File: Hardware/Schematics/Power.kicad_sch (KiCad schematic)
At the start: 26 parts, among them J7 USB_B_Micro, J8 Conn_01x02, U5 MT3608, U6 BQ25071, U7 TPS63900, U9 WE-TVS-82400102

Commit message: title block update
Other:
- title: Water Analyser Power -> LoRa Node Power
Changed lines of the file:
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@@
 	(paper "A4")
 	(title_block
-		(title "Water Analyser Power")
+		(title "LoRa Node Power")
 		(date "2025-11-28")
 		(rev "A")
@@
 		)
 		(instances
-			(project "demo wateranalyser"
+			(project "demo LoRa_Node"
 				(path "/3e989608-eeda-4a48-bc6c-c5e1d1678702/98bcb7c1-a14b-48e1-9268-def1b948ddb6"
 					(reference "#PWR061")
@@
 		)
 		(instances
-			(project "demo wateranalyser"
+			(project "demo LoRa_Node"
 				(path "/3e989608-eeda-4a48-bc6c-c5e1d1678702/98bcb7c1-a14b-48e1-9268-def1b948ddb6"
 					(reference "U6")
@@
 		)
 		(instances
-			(project "demo wateranalyser"
+			(project "demo LoRa_Node"
 				(path "/3e989608-eeda-4a48-bc6c-c5e1d1678702/98bcb7c1-a14b-48e1-9268-def1b948ddb6"
 					(reference "U9")
@@
 		)
 		(instances
-			(project "demo wateranalyser"
+			(project "demo LoRa_Node"
 				(path "/3e989608-eeda-4a48-bc6c-c5e1d1678702/98bcb7c1-a14b-48e1-9268-def1b948ddb6"
 					(reference "#PWR058")
@@
 		)
 		(instances
-			(project "demo wateranalyser"
+			(project "demo LoRa_Node"
 				(path "/3e989608-eeda-4a48-bc6c-c5e1d1678702/98bcb7c1-a14b-48e1-9268-def1b948ddb6"
 					(reference "#FLG01")
@@
 		)
 		(instances
-			(project "demo wateranalyser"
+			(project "demo LoRa_Node"
 				(path "/3e989608-eeda-4a48-bc6c-c5e1d1678702/98bcb7c1-a14b-48e1-9268-def1b948ddb6"
 					(reference "BT1")
@@
 		)
 		(instances
-			(project "demo wateranalyser"
+			(project "demo LoRa_Node"
 				(path "/3e989608-eeda-4a48-bc6c-c5e1d1678702/98bcb7c1-a14b-48e1-9268-def1b948ddb6"
 					(reference "R22")
@@
 		)
 		(instances
-			(project "demo wateranalyser"
+			(project "demo LoRa_Node"
 				(path "/3e989608-eeda-4a48-bc6c-c5e1d1678702/98bcb7c1-a14b-48e1-9268-def1b948ddb6"
 					(reference "C35")
@@
 		)
 		(instances
-			(project "demo wateranalyser"
+			(project "demo LoRa_Node"
 				(path "/3e989608-eeda-4a48-bc6c-c5e1d1678702/98bcb7c1-a14b-48e1-9268-def1b948ddb6"
 					(reference "#PWR064")
@@
 		)
 		(instances
-			(project "demo wateranalyser"
+			(project "demo LoRa_Node"
 				(path "/3e989608-eeda-4a48-bc6c-c5e1d1678702/98bcb7c1-a14b-48e1-9268-def1b948ddb6"
 					(reference "#PWR056")
@@
 		)
 		(instances
-			(project "demo wateranalyser"
+			(project "demo LoRa_Node"
 				(path "/3e989608-eeda-4a48-bc6c-c5e1d1678702/98bcb7c1-a14b-48e1-9268-def1b948ddb6"
 					(reference "#PWR055")
@@
 		)
 		(instances
-			(project "demo wateranalyser"
+			(project "demo LoRa_Node"
 				(path "/3e989608-eeda-4a48-bc6c-c5e1d1678702/98bcb7c1-a14b-48e1-9268-def1b948ddb6"
 					(reference "L7")
@@
 		)
 		(instances
-			(project "demo wateranalyser"
+			(project "demo LoRa_Node"
 				(path "/3e989608-eeda-4a48-bc6c-c5e1d1678702/98bcb7c1-a14b-48e1-9268-def1b948ddb6"
 					(reference "D9")
@@
 		)
 		(instances
-			(project "demo wateranalyser"
+			(project "demo LoRa_Node"
 				(path "/3e989608-eeda-4a48-bc6c-c5e1d1678702/98bcb7c1-a14b-48e1-9268-def1b948ddb6"
 					(reference "#PWR050")
@@
 		)
 		(instances
-			(project "demo wateranalyser"
+			(project "demo LoRa_Node"
 				(path "/3e989608-eeda-4a48-bc6c-c5e1d1678702/98bcb7c1-a14b-48e1-9268-def1b948ddb6"
 					(reference "#PWR057")
@@
 		)
 		(instances
-			(project "demo wateranalyser"
+			(project "demo LoRa_Node"
 				(path "/3e989608-eeda-4a48-bc6c-c5e1d1678702/98bcb7c1-a14b-48e1-9268-def1b948ddb6"
 					(reference "#FLG04")
@@
 		)
 		(instances
-			(project "demo wateranalyser"
+			(project "demo LoRa_Node"
 				(path "/3e989608-eeda-4a48-bc6c-c5e1d1678702/98bcb7c1-a14b-48e1-9268-def1b948ddb6"
 					(reference "R24")
@@
 		)
 		(instances
-			(project "demo wateranalyser"
+			(project "demo LoRa_Node"
 				(path "/3e989608-eeda-4a48-bc6c-c5e1d1678702/98bcb7c1-a14b-48e1-9268-def1b948ddb6"
 					(reference "R21")
@@
 		)
 		(instances
-			(project "demo wateranalyser"
+			(project "demo LoRa_Node"
 				(path "/3e989608-eeda-4a48-bc6c-c5e1d1678702/98bcb7c1-a14b-48e1-9268-def1b948ddb6"
 					(reference "#PWR048")
@@
 		)
 		(instances
-			(project "demo wateranalyser"
+			(project "demo LoRa_Node"
 				(path "/3e989608-eeda-4a48-bc6c-c5e1d1678702/98bcb7c1-a14b-48e1-9268-def1b948ddb6"
 					(reference "U7")
@@
 		)
 		(instances
-			(project "demo wateranalyser"
+			(project "demo LoRa_Node"
 				(path "/3e989608-eeda-4a48-bc6c-c5e1d1678702/98bcb7c1-a14b-48e1-9268-def1b948ddb6"
 					(reference "J7")
@@
 		)
 		(instances
-			(project "demo wateranalyser"
+			(project "demo LoRa_Node"
 				(path "/3e989608-eeda-4a48-bc6c-c5e1d1678702/98bcb7c1-a14b-48e1-9268-def1b948ddb6"
 					(reference "#PWR053")
@@
 		)
 		(instances
-			(project "demo wateranalyser"
+			(project "demo LoRa_Node"
 				(path "/3e989608-eeda-4a48-bc6c-c5e1d1678702/98bcb7c1-a14b-48e1-9268-def1b948ddb6"
 					(reference "#PWR047")
@@
 		)
 		(instances
-			(project "demo wateranalyser"
+			(project "demo LoRa_Node"
 				(path "/3e989608-eeda-4a48-bc6c-c5e1d1678702/98bcb7c1-a14b-48e1-9268-def1b948ddb6"
 					(reference "R19")
@@
 		)
 		(instances
-			(project "demo wateranalyser"
+			(project "demo LoRa_Node"
 				(path "/3e989608-eeda-4a48-bc6c-c5e1d1678702/98bcb7c1-a14b-48e1-9268-def1b948ddb6"
 					(reference "D8")
@@
 		)
 		(instances
-			(project "demo wateranalyser"
+			(project "demo LoRa_Node"
 				(path "/3e989608-eeda-4a48-bc6c-c5e1d1678702/98bcb7c1-a14b-48e1-9268-def1b948ddb6"
 					(reference "#PWR051")
@@
 		)
 		(instances
-			(project "demo wateranalyser"
+			(project "demo LoRa_Node"
 				(path "/3e989608-eeda-4a48-bc6c-c5e1d1678702/98bcb7c1-a14b-48e1-9268-def1b948ddb6"
 					(reference "#PWR060")
@@
 		)
 		(instances
-			(project "demo wateranalyser"
+			(project "demo LoRa_Node"
 				(path "/3e989608-eeda-4a48-bc6c-c5e1d1678702/98bcb7c1-a14b-48e1-9268-def1b948ddb6"
 					(reference "C34")
@@
 		)
 		(instances
-			(project "demo wateranalyser"
+			(project "demo LoRa_Node"
 				(path "/3e989608-eeda-4a48-bc6c-c5e1d1678702/98bcb7c1-a14b-48e1-9268-def1b948ddb6"
 					(reference "C37")
@@
 		)
 		(instances
-			(project "demo wateranalyser"
+			(project "demo LoRa_Node"
 				(path "/3e989608-eeda-4a48-bc6c-c5e1d1678702/98bcb7c1-a14b-48e1-9268-def1b948ddb6"
 					(reference "#PWR054")
@@
 		)
 		(instances
-			(project "demo wateranalyser"
+			(project "demo LoRa_Node"
 				(path "/3e989608-eeda-4a48-bc6c-c5e1d1678702/98bcb7c1-a14b-48e1-9268-def1b948ddb6"
 					(reference "#PWR049")
@@
 		)
 		(instances
-			(project "demo wateranalyser"
+			(project "demo LoRa_Node"
 				(path "/3e989608-eeda-4a48-bc6c-c5e1d1678702/98bcb7c1-a14b-48e1-9268-def1b948ddb6"
 					(reference "C32")
@@
 		)
 		(instances
-			(project "demo wateranalyser"
+			(project "demo LoRa_Node"
 				(path "/3e989608-eeda-4a48-bc6c-c5e1d1678702/98bcb7c1-a14b-48e1-9268-def1b948ddb6"
 					(reference "#PWR063")
@@
 		)
 		(instances
-			(project "demo wateranalyser"
+			(project "demo LoRa_Node"
 				(path "/3e989608-eeda-4a48-bc6c-c5e1d1678702/98bcb7c1-a14b-48e1-9268-def1b948ddb6"
 					(reference "R25")
@@
 		)
 		(instances
-			(project "demo wateranalyser"
+			(project "demo LoRa_Node"
 				(path "/3e989608-eeda-4a48-bc6c-c5e1d1678702/98bcb7c1-a14b-48e1-9268-def1b948ddb6"
 					(reference "#PWR052")
@@
 		)
 		(instances
-			(project "demo wateranalyser"
+			(project "demo LoRa_Node"
 				(path "/3e989608-eeda-4a48-bc6c-c5e1d1678702/98bcb7c1-a14b-48e1-9268-def1b948ddb6"
 					(reference "J8")
@@
 		)
 		(instances
-			(project "demo wateranalyser"
+			(project "demo LoRa_Node"
 				(path "/3e989608-eeda-4a48-bc6c-c5e1d1678702/98bcb7c1-a14b-48e1-9268-def1b948ddb6"
 					(reference "R20")
@@
 		)
 		(instances
-			(project "demo wateranalyser"
+			(project "demo LoRa_Node"
 				(path "/3e989608-eeda-4a48-bc6c-c5e1d1678702/98bcb7c1-a14b-48e1-9268-def1b948ddb6"
 					(reference "R27")
@@
 		)
 		(instances
-			(project "demo wateranalyser"
+			(project "demo LoRa_Node"
 				(path "/3e989608-eeda-4a48-bc6c-c5e1d1678702/98bcb7c1-a14b-48e1-9268-def1b948ddb6"
 					(reference "#PWR062")
@@
 		)
 		(instances
-			(project "demo wateranalyser"
+			(project "demo LoRa_Node"
 				(path "/3e989608-eeda-4a48-bc6c-c5e1d1678702/98bcb7c1-a14b-48e1-9268-def1b948ddb6"
 					(reference "#PWR059")
@@
 		)
 		(instances
-			(project "demo wateranalyser"
+			(project "demo LoRa_Node"
 				(path "/3e989608-eeda-4a48-bc6c-c5e1d1678702/98bcb7c1-a14b-48e1-9268-def1b948ddb6"
 					(reference "L8")
@@
 		)
 		(instances
-			(project "demo wateranalyser"
+			(project "demo LoRa_Node"
 				(path "/3e989608-eeda-4a48-bc6c-c5e1d1678702/98bcb7c1-a14b-48e1-9268-def1b948ddb6"
 					(reference "U5")
@@
 		)
 		(instances
-			(project "demo wateranalyser"
+			(project "demo LoRa_Node"
 				(path "/3e989608-eeda-4a48-bc6c-c5e1d1678702/98bcb7c1-a14b-48e1-9268-def1b948ddb6"
 					(reference "C38")
@@
 		)
 		(instances
-			(project "demo wateranalyser"
+			(project "demo LoRa_Node"
 				(path "/3e989608-eeda-4a48-bc6c-c5e1d1678702/98bcb7c1-a14b-48e1-9268-def1b948ddb6"
 					(reference "C36")
@@
 		)
 		(instances
-			(project "demo wateranalyser"
+			(project "demo LoRa_Node"
 				(path "/3e989608-eeda-4a48-bc6c-c5e1d1678702/98bcb7c1-a14b-48e1-9268-def1b948ddb6"
 					(reference "C33")
@@
 		)
 		(instances
-			(project "demo wateranalyser"
+			(project "demo LoRa_Node"
 				(path "/3e989608-eeda-4a48-bc6c-c5e1d1678702/98bcb7c1-a14b-48e1-9268-def1b948ddb6"
 					(reference "R23")

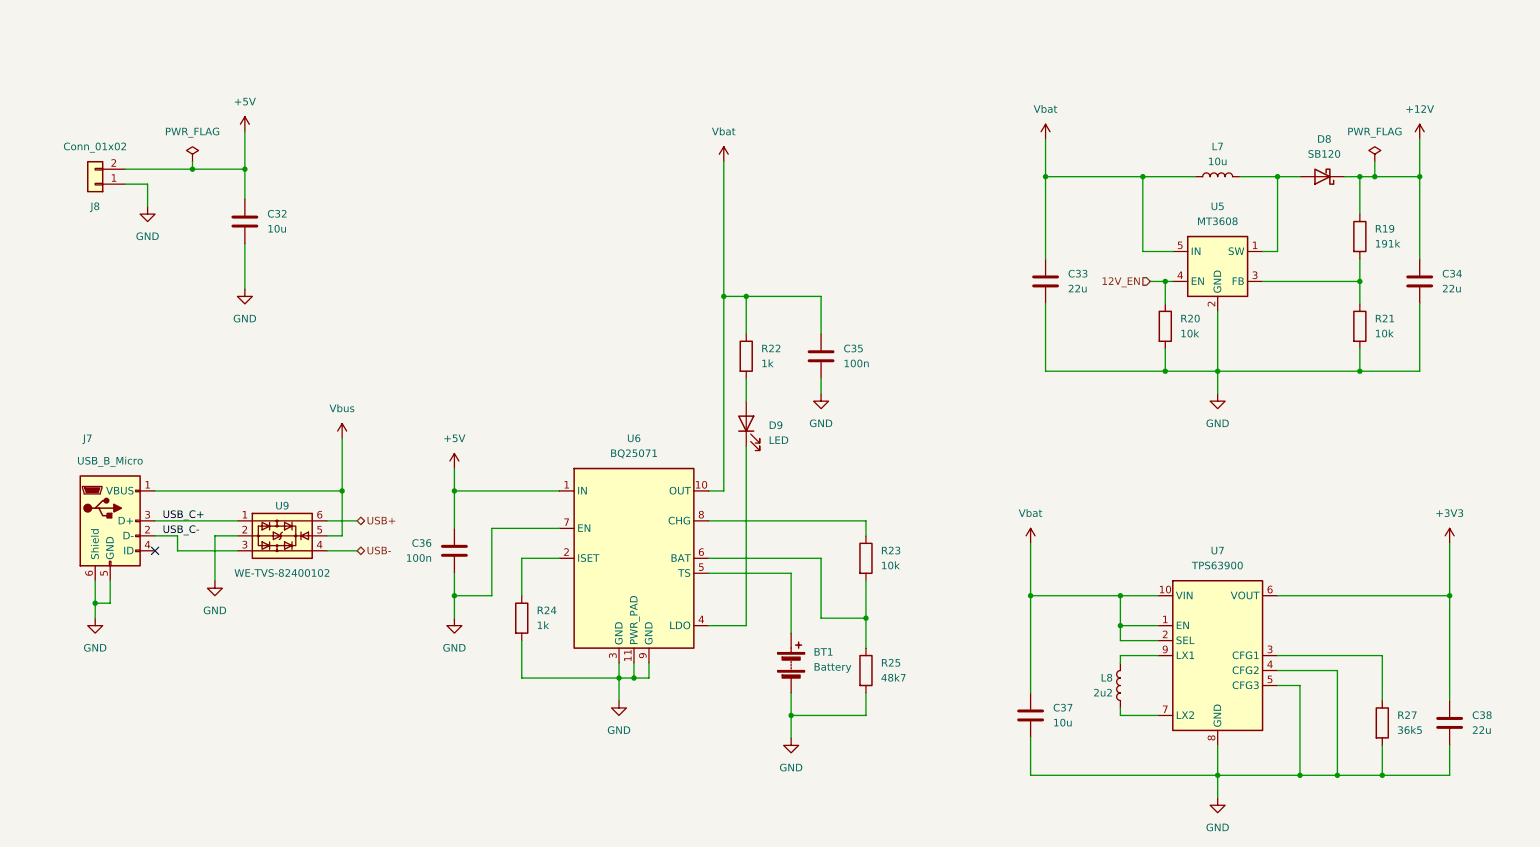
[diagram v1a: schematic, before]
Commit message: adjustment to the power section
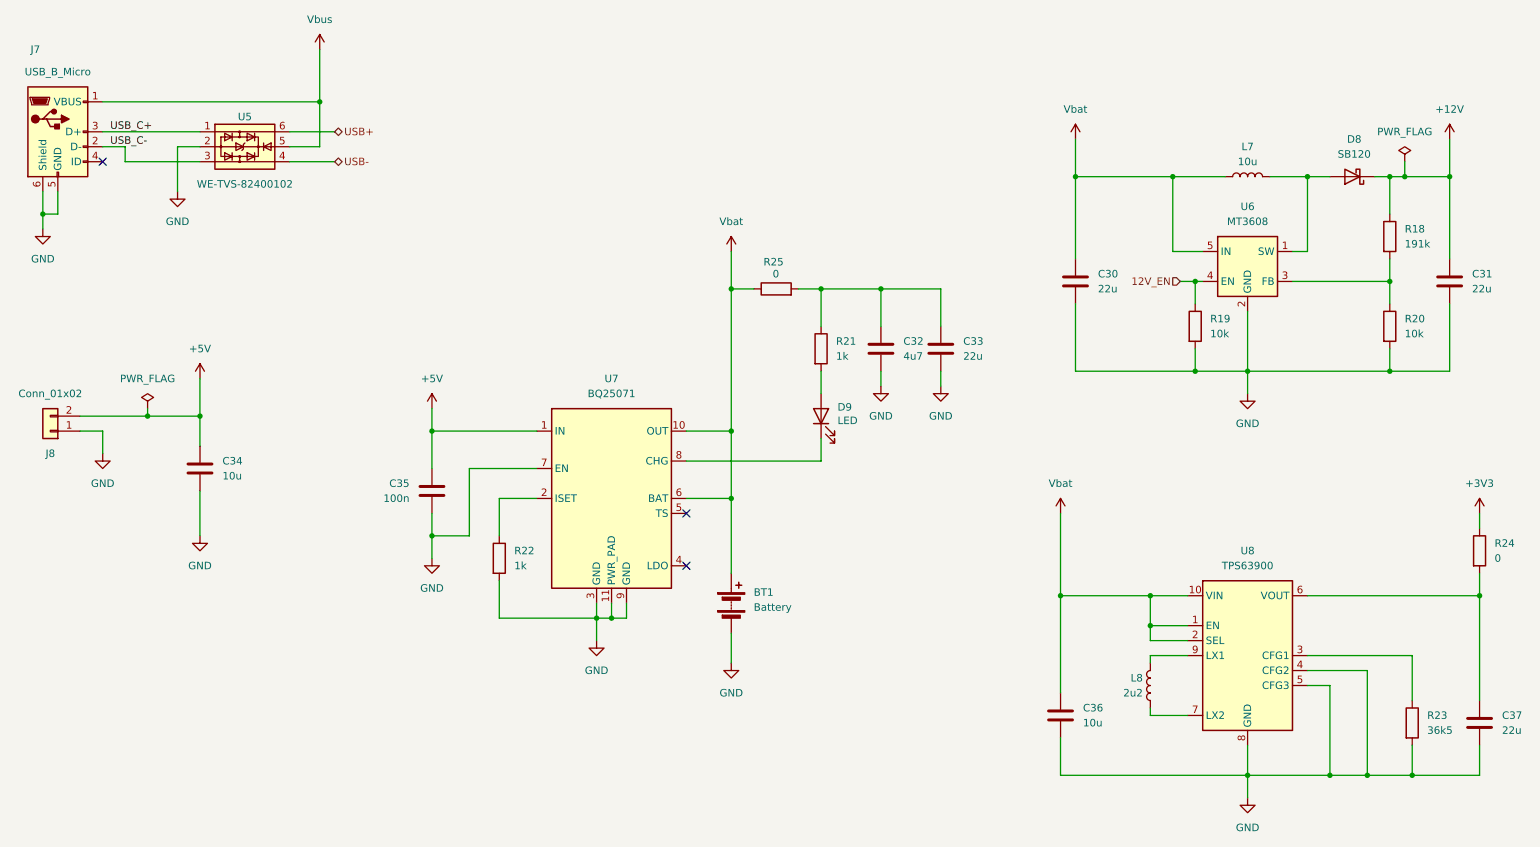
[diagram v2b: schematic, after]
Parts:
- removed R23: 10k, Resistor_SMD:R_0603_1608Metric, symbol Device:R
- added C33: 22u, Capacitor_SMD:C_0603_1608Metric, symbol Device:C
- added R24: 0, Resistor_SMD:R_0603_1608Metric, symbol Device:R
- C32: renamed from C35; value 100n -> 4u7
- R25: value 48k7 -> 0
- renumbered C33 to C30, C34 to C31, C32 to C34, C36 to C35, C37 to C36, C38 to C37, R19 to R18, R20 to R19, R21 to R20, R22 to R21, R24 to R22, R27 to R23, U9 to U5, U5 to U6, U6 to U7, U7 to U8
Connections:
- net +3V3: now also R24.1; no longer C37.1, U8.6 (VOUT)
- net GND: now also C33.2; no longer R25.2
- net Vbat: now also BT1.1 (+), R25.1, U7.6 (BAT); no longer C32.1, R21.1
- net at U7.4 (LDO): no longer D9.1 (K)
- net at U7.5 (TS): no longer BT1.1 (+)
- net at U7.8 (CHG): now also D9.1 (K)
- new net: C32.1, C33.1, R21.1, R25.2
- new net: C37.1, R24.2, U8.6 (VOUT)
- no-connect marks 1 -> 3
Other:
- moved on the sheet: BT1, C30, C31, C32, C34, C35, C36, C37, D8, D9, J7, J8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

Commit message: final hardware V1
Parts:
- added C38: 100n, Capacitor_SMD:C_0603_1608Metric, symbol Device:C
- added R26: 100k, Resistor_SMD:R_0603_1608Metric, symbol Device:R
- added R27: 490k, Resistor_SMD:R_0603_1608Metric, symbol Device:R
- R19: value 10k -> 100k
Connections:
- net GND: now also C38.2, R26.2
- net at U7.4 (LDO): now also C38.1, R27.1
- net at U7.5 (TS): now also R26.1, R27.2
- no-connect marks 3 -> 1
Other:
- moved on the sheet: BT1, C32, C33, D9, R21, R25
